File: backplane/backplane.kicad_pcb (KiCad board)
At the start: 2 copper layers, 99.1 x 99.1 mm, 10 parts, among them J8 Barrel_Jack_Switch, U1 7805

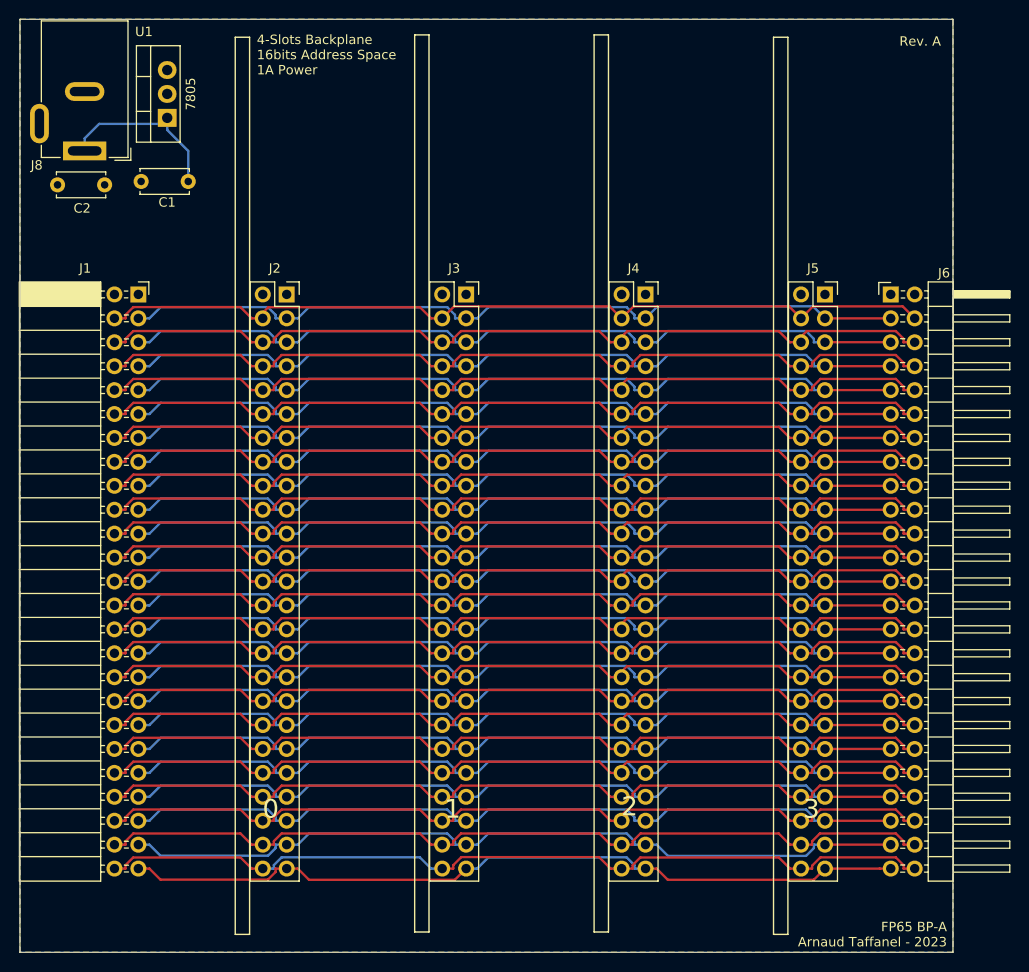
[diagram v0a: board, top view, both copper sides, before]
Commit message: Add mounting/alignement holes to backplane
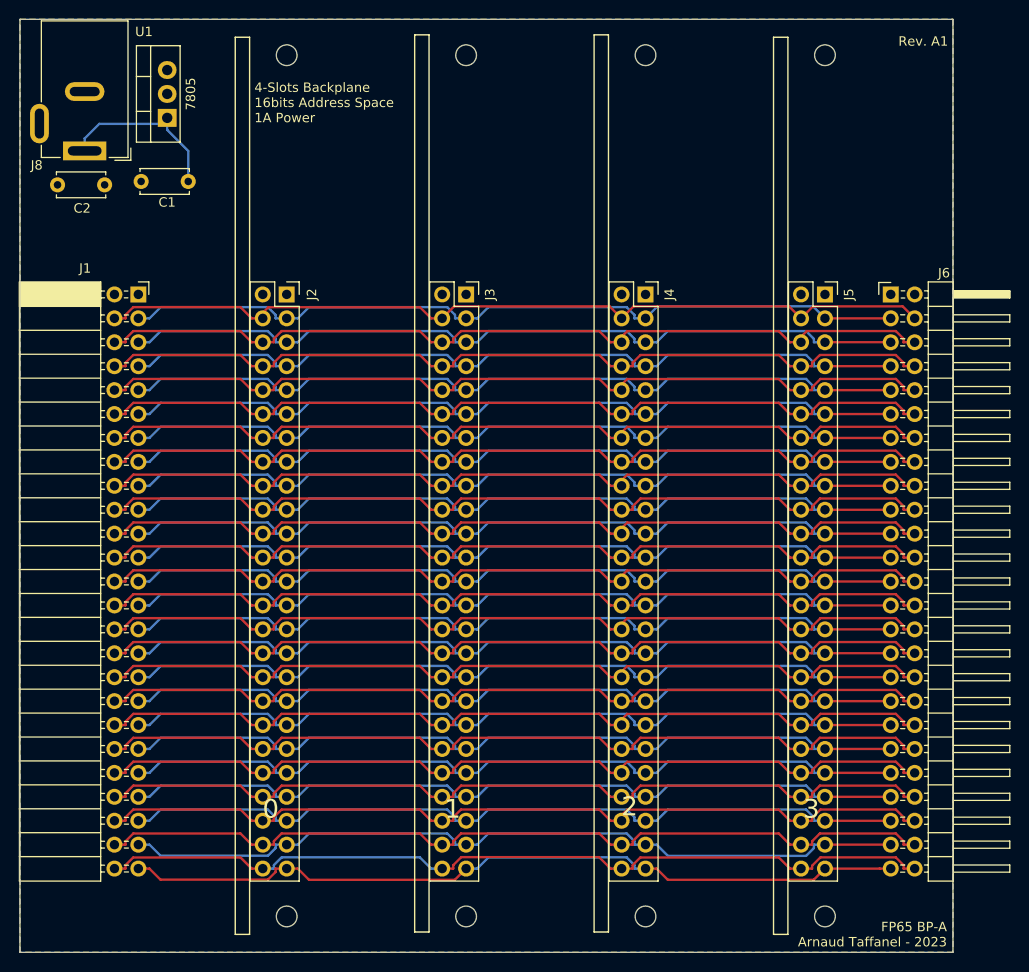
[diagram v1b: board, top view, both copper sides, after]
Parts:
- added REF**: MountingHole_2.2mm_M2, MountingHole:MountingHole_2.2mm_M2, F.Cu at (133.6, 122.0)
- added REF**: MountingHole_2.2mm_M2, MountingHole:MountingHole_2.2mm_M2, F.Cu at (114.6, 30.6)
- added REF**: MountingHole_2.2mm_M2, MountingHole:MountingHole_2.2mm_M2, F.Cu at (171.7, 122.0)
- added REF**: MountingHole_2.2mm_M2, MountingHole:MountingHole_2.2mm_M2, F.Cu at (114.6, 122.0)
- added REF**: MountingHole_2.2mm_M2, MountingHole:MountingHole_2.2mm_M2, F.Cu at (152.7, 122.0)
- added REF**: MountingHole_2.2mm_M2, MountingHole:MountingHole_2.2mm_M2, F.Cu at (171.7, 30.6)
- added REF**: MountingHole_2.2mm_M2, MountingHole:MountingHole_2.2mm_M2, F.Cu at (133.6, 30.6)
- added REF**: MountingHole_2.2mm_M2, MountingHole:MountingHole_2.2mm_M2, F.Cu at (152.7, 30.6)
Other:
- board text added: "Rev. A1"
- board text removed: "Rev. A"
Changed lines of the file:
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@@
   (net 51 "+12V")
   (net 52 "unconnected-(J8-Pad3)")
+  (footprint "MountingHole:MountingHole_2.2mm_M2" (layer "F.Cu")
+    (at 133.604 122.047)
+    (descr "Mounting Hole 2.2mm, no annular, M2")
+    (tags "mounting hole 2.2mm no annular m2")
+    (attr exclude_from_pos_files exclude_from_bom)
+    (fp_text reference "REF**" (at 0 -3.2) (layer "F.SilkS") hide
+        (effects (font (size 1 1) (thickness 0.15)))
+    )
+    (fp_text value "MountingHole_2.2mm_M2" (at 0 3.2) (layer "F.Fab")
+        (effects (font (size 1 1) (thickness 0.15)))
+    )
+    (fp_text user "${REFERENCE}" (at 0 0) (layer "F.Fab")
+        (effects (font (size 1 1) (thickness 0.15)))
+    )
+    (fp_circle (center 0 0) (end 2.2 0)
+      (stroke (width 0.15) (type solid)) (fill none) (layer "Cmts.User"))
+    (fp_circle (center 0 0) (end 2.45 0)
+      (stroke (width 0.05) (type solid)) (fill none) (layer "F.CrtYd"))
+    (pad "" np_thru_hole circle (at 0 0) (size 2.2 2.2) (drill 2.2) (layers "*.Cu" "*.Mask"))
+  )
+  (footprint "MountingHole:MountingHole_2.2mm_M2" (layer "F.Cu")
+    (at 114.554 30.607)
+    (descr "Mounting Hole 2.2mm, no annular, M2")
+    (tags "mounting hole 2.2mm no annular m2")
+    (attr exclude_from_pos_files exclude_from_bom)
+    (fp_text reference "REF**" (at 0 -3.2) (layer "F.SilkS") hide
+        (effects (font (size 1 1) (thickness 0.15)))
+    )
+    (fp_text value "MountingHole_2.2mm_M2" (at 0 3.2) (layer "F.Fab")
+        (effects (font (size 1 1) (thickness 0.15)))
+    )
+    (fp_text user "${REFERENCE}" (at 0 0) (layer "F.Fab")
+        (effects (font (size 1 1) (thickness 0.15)))
+    )
+    (fp_circle (center 0 0) (end 2.2 0)
+      (stroke (width 0.15) (type solid)) (fill none) (layer "Cmts.User"))
+    (fp_circle (center 0 0) (end 2.45 0)
+      (stroke (width 0.05) (type solid)) (fill none) (layer "F.CrtYd"))
+    (pad "" np_thru_hole circle (at 0 0) (size 2.2 2.2) (drill 2.2) (layers "*.Cu" "*.Mask"))
+  )
   (footprint "Connector_PinHeader_2.54mm:PinHeader_2x25_P2.54mm_Horizontal" (layer "F.Cu")
     (at 178.689 56.007)
@@
     )
   )
+  (footprint "MountingHole:MountingHole_2.2mm_M2" (layer "F.Cu")
+    (at 171.704 122.047)
+    (descr "Mounting Hole 2.2mm, no annular, M2")
+    (tags "mounting hole 2.2mm no annular m2")
+    (attr exclude_from_pos_files exclude_from_bom)
+    (fp_text reference "REF**" (at 0 -3.2) (layer "F.SilkS") hide
+        (effects (font (size 1 1) (thickness 0.15)))
+    )
+    (fp_text value "MountingHole_2.2mm_M2" (at 0 3.2) (layer "F.Fab")
+        (effects (font (size 1 1) (thickness 0.15)))
+    )
+    (fp_text user "${REFERENCE}" (at 0 0) (layer "F.Fab")
+        (effects (font (size 1 1) (thickness 0.15)))
+    )
+    (fp_circle (center 0 0) (end 2.2 0)
+      (stroke (width 0.15) (type solid)) (fill none) (layer "Cmts.User"))
+    (fp_circle (center 0 0) (end 2.45 0)
+      (stroke (width 0.05) (type solid)) (fill none) (layer "F.CrtYd"))
+    (pad "" np_thru_hole circle (at 0 0) (size 2.2 2.2) (drill 2.2) (layers "*.Cu" "*.Mask"))
+  )
+  (footprint "MountingHole:MountingHole_2.2mm_M2" (layer "F.Cu")
+    (at 114.554 122.047)
+    (descr "Mounting Hole 2.2mm, no annular, M2")
+    (tags "mounting hole 2.2mm no annular m2")
+    (attr exclude_from_pos_files exclude_from_bom)
+    (fp_text reference "REF**" (at 0 -3.2) (layer "F.SilkS") hide
+        (effects (font (size 1 1) (thickness 0.15)))
+    )
+    (fp_text value "MountingHole_2.2mm_M2" (at 0 3.2) (layer "F.Fab")
+        (effects (font (size 1 1) (thickness 0.15)))
+    )
+    (fp_text user "${REFERENCE}" (at 0 0) (layer "F.Fab")
+        (effects (font (size 1 1) (thickness 0.15)))
+    )
+    (fp_circle (center 0 0) (end 2.2 0)
+      (stroke (width 0.15) (type solid)) (fill none) (layer "Cmts.User"))
+    (fp_circle (center 0 0) (end 2.45 0)
+      (stroke (width 0.05) (type solid)) (fill none) (layer "F.CrtYd"))
+    (pad "" np_thru_hole circle (at 0 0) (size 2.2 2.2) (drill 2.2) (layers "*.Cu" "*.Mask"))
+  )
   (footprint "Connector_PinSocket_2.54mm:PinSocket_2x25_P2.54mm_Vertical" (layer "F.Cu")
     (at 171.704 56.007)
@@
     (property "Sheetname" "")
     (attr through_hole)
-    (fp_text reference "J5" (at -1.27 -2.77) (layer "F.SilkS")
+    (fp_text reference "J5" (at 2.54 0 -90) (layer "F.SilkS")
         (effects (font (size 1 1) (thickness 0.15)))
     )
@@
     (property "Sheetname" "")
     (attr through_hole)
-    (fp_text reference "J4" (at -1.27 -2.77) (layer "F.SilkS")
+    (fp_text reference "J4" (at 2.54 0 -90) (layer "F.SilkS")
         (effects (font (size 1 1) (thickness 0.15)))
     )
@@
     )
   )
+  (footprint "MountingHole:MountingHole_2.2mm_M2" (layer "F.Cu")
+    (at 152.654 122.047)
+    (descr "Mounting Hole 2.2mm, no annular, M2")
+    (tags "mounting hole 2.2mm no annular m2")
+    (attr exclude_from_pos_files exclude_from_bom)
+    (fp_text reference "REF**" (at 0 -3.2) (layer "F.SilkS") hide
+        (effects (font (size 1 1) (thickness 0.15)))
+    )
+    (fp_text value "MountingHole_2.2mm_M2" (at 0 3.2) (layer "F.Fab")
+        (effects (font (size 1 1) (thickness 0.15)))
+    )
+    (fp_text user "${REFERENCE}" (at 0 0) (layer "F.Fab")
+        (effects (font (size 1 1) (thickness 0.15)))
+    )
+    (fp_circle (center 0 0) (end 2.2 0)
+      (stroke (width 0.15) (type solid)) (fill none) (layer "Cmts.User"))
+    (fp_circle (center 0 0) (end 2.45 0)
+      (stroke (width 0.05) (type solid)) (fill none) (layer "F.CrtYd"))
+    (pad "" np_thru_hole circle (at 0 0) (size 2.2 2.2) (drill 2.2) (layers "*.Cu" "*.Mask"))
+  )
+  (footprint "MountingHole:MountingHole_2.2mm_M2" (layer "F.Cu")
+    (at 171.704 30.607)
+    (descr "Mounting Hole 2.2mm, no annular, M2")
+    (tags "mounting hole 2.2mm no annular m2")
+    (attr exclude_from_pos_files exclude_from_bom)
+    (fp_text reference "REF**" (at 0 -3.2) (layer "F.SilkS") hide
+        (effects (font (size 1 1) (thickness 0.15)))
+    )
+    (fp_text value "MountingHole_2.2mm_M2" (at 0 3.2) (layer "F.Fab")
+        (effects (font (size 1 1) (thickness 0.15)))
+    )
+    (fp_text user "${REFERENCE}" (at 0 0) (layer "F.Fab")
+        (effects (font (size 1 1) (thickness 0.15)))
+    )
+    (fp_circle (center 0 0) (end 2.2 0)
+      (stroke (width 0.15) (type solid)) (fill none) (layer "Cmts.User"))
+    (fp_circle (center 0 0) (end 2.45 0)
+      (stroke (width 0.05) (type solid)) (fill none) (layer "F.CrtYd"))
+    (pad "" np_thru_hole circle (at 0 0) (size 2.2 2.2) (drill 2.2) (layers "*.Cu" "*.Mask"))
+  )
   (footprint "Connector_PinSocket_2.54mm:PinSocket_2x25_P2.54mm_Vertical" (layer "F.Cu")
     (at 114.554 56.007)
@@
     (property "Sheetname" "")
     (attr through_hole)
-    (fp_text reference "J2" (at -1.27 -2.77) (layer "F.SilkS")
+    (fp_text reference "J2" (at 2.667 0 90) (layer "F.SilkS")
         (effects (font (size 1 1) (thickness 0.15)))
     )
@@
     )
   )
+  (footprint "MountingHole:MountingHole_2.2mm_M2" (layer "F.Cu")
+    (at 133.604 30.607)
+    (descr "Mounting Hole 2.2mm, no annular, M2")
+    (tags "mounting hole 2.2mm no annular m2")
+    (attr exclude_from_pos_files exclude_from_bom)
+    (fp_text reference "REF**" (at 0 -3.2) (layer "F.SilkS") hide
+        (effects (font (size 1 1) (thickness 0.15)))
+    )
+    (fp_text value "MountingHole_2.2mm_M2" (at 0 3.2) (layer "F.Fab")
+        (effects (font (size 1 1) (thickness 0.15)))
+    )
+    (fp_text user "${REFERENCE}" (at 0 0) (layer "F.Fab")
+        (effects (font (size 1 1) (thickness 0.15)))
+    )
+    (fp_circle (center 0 0) (end 2.2 0)
+      (stroke (width 0.15) (type solid)) (fill none) (layer "Cmts.User"))
+    (fp_circle (center 0 0) (end 2.45 0)
+      (stroke (width 0.05) (type solid)) (fill none) (layer "F.CrtYd"))
+    (pad "" np_thru_hole circle (at 0 0) (size 2.2 2.2) (drill 2.2) (layers "*.Cu" "*.Mask"))
+  )
   (footprint "Package_TO_SOT_THT:TO-220-3_Vertical" (layer "F.Cu")
     (at 101.869 37.261 90)
@@
     (property "Sheetname" "")
     (attr through_hole)
-    (fp_text reference "J3" (at -1.27 -2.77) (layer "F.SilkS")
+    (fp_text reference "J3" (at 2.54 0 90) (layer "F.SilkS")
         (effects (font (size 1 1) (thickness 0.15)))
     )
@@
     )
   )
+  (footprint "MountingHole:MountingHole_2.2mm_M2" (layer "F.Cu")
+    (at 152.654 30.607)
+    (descr "Mounting Hole 2.2mm, no annular, M2")
+    (tags "mounting hole 2.2mm no annular m2")
+    (attr exclude_from_pos_files exclude_from_bom)
+    (fp_text reference "REF**" (at 0 -3.2) (layer "F.SilkS") hide
+        (effects (font (size 1 1) (thickness 0.15)))
+    )
+    (fp_text value "MountingHole_2.2mm_M2" (at 0 3.2) (layer "F.Fab")
+        (effects (font (size 1 1) (thickness 0.15)))
+    )
+    (fp_text user "${REFERENCE}" (at 0 0) (layer "F.Fab")
+        (effects (font (size 1 1) (thickness 0.15)))
+    )
+    (fp_circle (center 0 0) (end 2.2 0)
+      (stroke (width 0.15) (type solid)) (fill none) (layer "Cmts.User"))
+    (fp_circle (center 0 0) (end 2.45 0)
+      (stroke (width 0.05) (type solid)) (fill none) (layer "F.CrtYd"))
+    (pad "" np_thru_hole circle (at 0 0) (size 2.2 2.2) (drill 2.2) (layers "*.Cu" "*.Mask"))
+  )
   (gr_line (start 167.767 123.952) (end 166.243 123.952)
     (stroke (width 0.15) (type default)) (layer "F.SilkS"))
@@
   (gr_line (start 185.293 26.797) (end 185.293 125.857)
     (stroke (width 0.1) (type default)) (layer "Edge.Cuts"))
-  (gr_text "Rev. A" (at 184.023 29.718) (layer "F.SilkS")
+  (gr_text "Rev. A1" (at 184.785 29.718) (layer "F.SilkS")
     (effects (font (size 1 1) (thickness 0.15)) (justify right bottom))
   )
@@
     (effects (font (size 2 2) (thickness 0.15)) (justify left bottom))
   )
-  (gr_text "4-Slots Backplane\n16bits Address Space\n1A Power" (at 111.379 32.766) (layer "F.SilkS")
+  (gr_text "4-Slots Backplane\n16bits Address Space\n1A Power" (at 111.125 37.846) (layer "F.SilkS")
     (effects (font (size 1 1) (thickness 0.15)) (justify left bottom))
   )
